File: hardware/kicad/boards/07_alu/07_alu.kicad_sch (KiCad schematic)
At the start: 0 parts

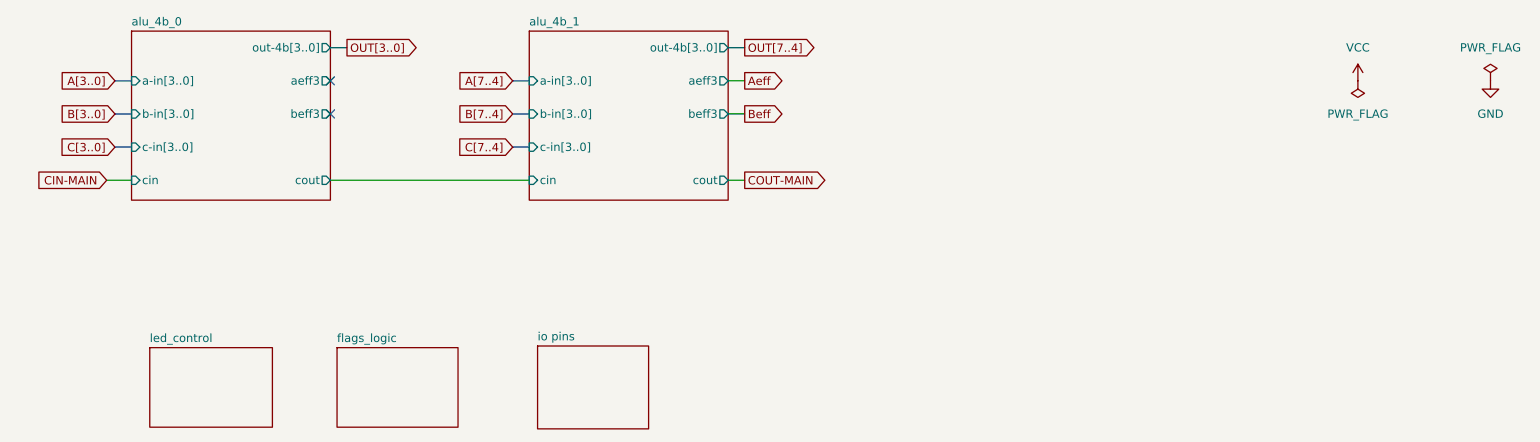
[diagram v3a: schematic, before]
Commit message: feat: route 8b ALU slice and annotate pending final signoff 🎉🎉
Highlights:
- 0 ERC/DRC errors
- 0 Unrouted nets
- 2345 track segments
- 388 vias after cleanup
- 760 pads
- 18 core 74xx chips
- 7 flag 74xx chips

Pending additional confirmation of hardware-simulation faithfulness and fidelity.
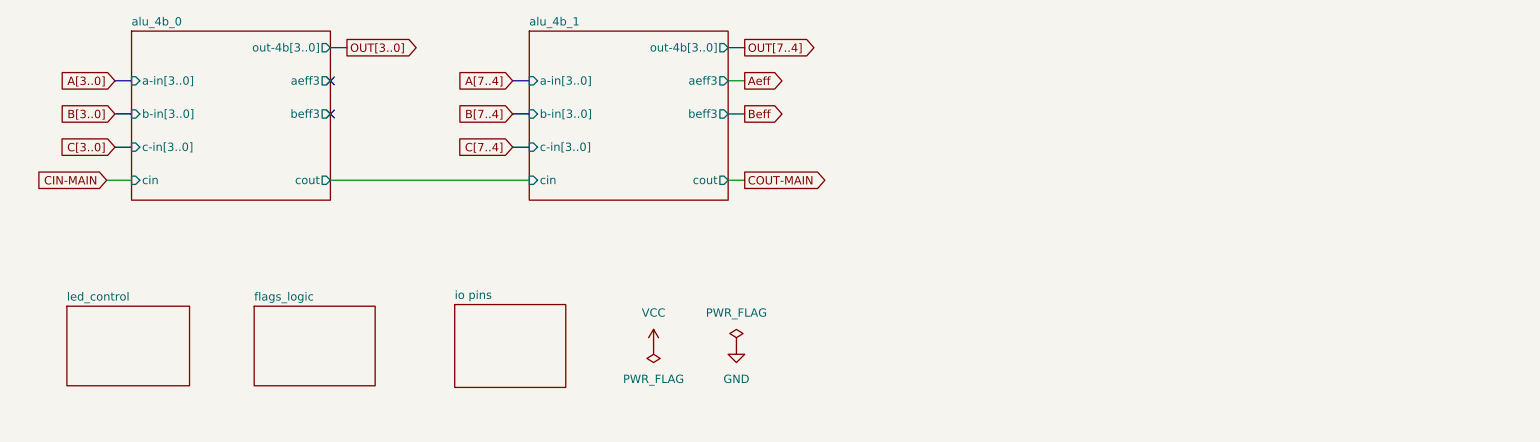
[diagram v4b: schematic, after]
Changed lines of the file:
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@@
 	(generator "eeschema")
 	(generator_version "10.0")
-	(paper "A4")
+	(paper "A5")
 	(no_connect
 		(at 63.5 40.64)
@@
 	(symbol
 		(lib_id "power:PWR_FLAG")
-		(at 220.98 35.56 180)
+		(at 125.73 76.2 0)
 		(unit 1)
 		(body_style 1)
@@
 		(dnp no)
 		(fields_autoplaced yes)
-		(property "Reference" "#FLG02"
-			(at 220.98 37.465 0)
+		(property "Reference" "#FLG01"
+			(at 125.73 74.295 0)
 			(hide yes)
 			(show_name no)
@@
 		)
 		(property "Value" "PWR_FLAG"
-			(at 220.98 40.64 0)
+			(at 125.73 71.12 0)
 			(show_name no)
 			(do_not_autoplace no)
@@
 		)
 		(property "Footprint" ""
-			(at 220.98 35.56 0)
+			(at 125.73 76.2 0)
 			(hide yes)
 			(show_name no)
@@
 		)
 		(property "Datasheet" ""
-			(at 220.98 35.56 0)
+			(at 125.73 76.2 0)
 			(hide yes)
 			(show_name no)
@@
 		)
 		(property "Description" "Special symbol for telling ERC where power comes from"
-			(at 220.98 35.56 0)
+			(at 125.73 76.2 0)
 			(hide yes)
 			(show_name no)
@@
 			(project "07_alu"
 				(path "/bf03590f-4078-420b-ac5f-55731d384371"
-					(reference "#FLG02")
+					(reference "#FLG01")
 					(unit 1)
 				)
@@
 	)
 	(symbol
-		(lib_id "power:VCC")
-		(at 220.98 35.56 0)
+		(lib_id "power:PWR_FLAG")
+		(at 113.03 76.2 180)
 		(unit 1)
 		(body_style 1)
@@
 		(dnp no)
 		(fields_autoplaced yes)
-		(property "Reference" "#PWR01"
-			(at 220.98 39.37 0)
-			(hide yes)
-			(show_name no)
-			(do_not_autoplace no)
-			(effects
-				(font
-					(size 1.27 1.27)
-				)
-			)
-		)
-		(property "Value" "VCC"
-			(at 220.98 30.48 0)
+		(property "Reference" "#FLG02"
+			(at 113.03 78.105 0)
+			(hide yes)
+			(show_name no)
+			(do_not_autoplace no)
+			(effects
+				(font
+					(size 1.27 1.27)
+				)
+			)
+		)
+		(property "Value" "PWR_FLAG"
+			(at 113.03 81.28 0)
 			(show_name no)
 			(do_not_autoplace no)
@@
 		)
 		(property "Footprint" ""
-			(at 220.98 35.56 0)
+			(at 113.03 76.2 0)
 			(hide yes)
 			(show_name no)
@@
 		)
 		(property "Datasheet" ""
-			(at 220.98 35.56 0)
-			(hide yes)
-			(show_name no)
-			(do_not_autoplace no)
-			(effects
-				(font
-					(size 1.27 1.27)
-				)
-			)
-		)
-		(property "Description" "Power symbol creates a global label with name \"VCC\""
-			(at 220.98 35.56 0)
+			(at 113.03 76.2 0)
+			(hide yes)
+			(show_name no)
+			(do_not_autoplace no)
+			(effects
+				(font
+					(size 1.27 1.27)
+				)
+			)
+		)
+		(property "Description" "Special symbol for telling ERC where power comes from"
+			(at 113.03 76.2 0)
 			(hide yes)
 			(show_name no)
@@
 			(project "07_alu"
 				(path "/bf03590f-4078-420b-ac5f-55731d384371"
-					(reference "#PWR01")
+					(reference "#FLG02")
 					(unit 1)
 				)
@@
 	)
 	(symbol
-		(lib_id "power:GND")
-		(at 241.3 35.56 0)
+		(lib_id "power:VCC")
+		(at 113.03 76.2 0)
 		(unit 1)
 		(body_style 1)
@@
 		(dnp no)
 		(fields_autoplaced yes)
-		(property "Reference" "#PWR02"
-			(at 241.3 41.91 0)
-			(hide yes)
-			(show_name no)
-			(do_not_autoplace no)
-			(effects
-				(font
-					(size 1.27 1.27)
-				)
-			)
-		)
-		(property "Value" "GND"
-			(at 241.3 40.64 0)
+		(property "Reference" "#PWR01"
+			(at 113.03 80.01 0)
+			(hide yes)
+			(show_name no)
+			(do_not_autoplace no)
+			(effects
+				(font
+					(size 1.27 1.27)
+				)
+			)
+		)
+		(property "Value" "VCC"
+			(at 113.03 71.12 0)
 			(show_name no)
 			(do_not_autoplace no)
@@
 		)
 		(property "Footprint" ""
-			(at 241.3 35.56 0)
+			(at 113.03 76.2 0)
 			(hide yes)
 			(show_name no)
@@
 		)
 		(property "Datasheet" ""
-			(at 241.3 35.56 0)
-			(hide yes)
-			(show_name no)
-			(do_not_autoplace no)
-			(effects
-				(font
-					(size 1.27 1.27)
-				)
-			)
-		)
-		(property "Description" "Power symbol creates a global label with name \"GND\" , ground"
-			(at 241.3 35.56 0)
+			(at 113.03 76.2 0)
+			(hide yes)
+			(show_name no)
+			(do_not_autoplace no)
+			(effects
+				(font
+					(size 1.27 1.27)
+				)
+			)
+		)
+		(property "Description" "Power symbol creates a global label with name \"VCC\""
+			(at 113.03 76.2 0)
 			(hide yes)
 			(show_name no)
@@
 			(project "07_alu"
 				(path "/bf03590f-4078-420b-ac5f-55731d384371"
-					(reference "#PWR02")
+					(reference "#PWR01")
 					(unit 1)
 				)
@@
 	)
 	(symbol
-		(lib_id "power:PWR_FLAG")
-		(at 241.3 35.56 0)
+		(lib_id "power:GND")
+		(at 125.73 76.2 0)
 		(unit 1)
 		(body_style 1)
@@
 		(dnp no)
 		(fields_autoplaced yes)
-		(property "Reference" "#FLG01"
-			(at 241.3 33.655 0)
-			(hide yes)
-			(show_name no)
-			(do_not_autoplace no)
-			(effects
-				(font
-					(size 1.27 1.27)
-				)
-			)
-		)
-		(property "Value" "PWR_FLAG"
-			(at 241.3 30.48 0)
+		(property "Reference" "#PWR02"
+			(at 125.73 82.55 0)
+			(hide yes)
+			(show_name no)
+			(do_not_autoplace no)
+			(effects
+				(font
+					(size 1.27 1.27)
+				)
+			)
+		)
+		(property "Value" "GND"
+			(at 125.73 81.28 0)
 			(show_name no)
 			(do_not_autoplace no)
@@
 		)
 		(property "Footprint" ""
-			(at 241.3 35.56 0)
+			(at 125.73 76.2 0)
 			(hide yes)
 			(show_name no)
@@
 		)
 		(property "Datasheet" ""
-			(at 241.3 35.56 0)
-			(hide yes)
-			(show_name no)
-			(do_not_autoplace no)
-			(effects
-				(font
-					(size 1.27 1.27)
-				)
-			)
-		)
-		(property "Description" "Special symbol for telling ERC where power comes from"
-			(at 241.3 35.56 0)
+			(at 125.73 76.2 0)
+			(hide yes)
+			(show_name no)
+			(do_not_autoplace no)
+			(effects
+				(font
+					(size 1.27 1.27)
+				)
+			)
+		)
+		(property "Description" "Power symbol creates a global label with name \"GND\" , ground"
+			(at 125.73 76.2 0)
 			(hide yes)
 			(show_name no)
@@
 			(project "07_alu"
 				(path "/bf03590f-4078-420b-ac5f-55731d384371"
-					(reference "#FLG01")
+					(reference "#PWR02")
 					(unit 1)
 				)
@@
 	)
 	(sheet
-		(at 35.814 76.454)
+		(at 23.114 70.104)
 		(size 18.796 12.192)
 		(exclude_from_sim no)
@@
 		)
 		(property "Sheetname" "led_control"
-			(at 35.814 75.7424 0)
+			(at 23.114 69.3924 0)
 			(show_name no)
 			(do_not_autoplace no)
@@
 		)
 		(property "Sheetfile" "led_unit.kicad_sch"
-			(at 35.814 89.2306 0)
+			(at 23.114 82.8806 0)
 			(hide yes)
 			(show_name no)
@@
 	)
 	(sheet
-		(at 64.516 76.454)
+		(at 51.816 70.104)
 		(size 18.542 12.192)
 		(exclude_from_sim no)
@@
 		)
 		(property "Sheetname" "flags_logic"
-			(at 64.516 75.7424 0)
+			(at 51.816 69.3924 0)
 			(show_name no)
 			(do_not_autoplace no)
@@
 		)
 		(property "Sheetfile" "flags_logic.kicad_sch"
-			(at 64.516 89.2306 0)
+			(at 51.816 82.8806 0)
 			(hide yes)
 			(show_name no)
@@
 	)
 	(sheet
-		(at 95.25 76.2)
+		(at 82.55 69.85)
 		(size 17.018 12.7)
 		(exclude_from_sim no)
@@
 		)
 		(property "Sheetname" "io pins"
-			(at 95.25 75.4884 0)
+			(at 82.55 69.1384 0)
 			(show_name no)
 			(do_not_autoplace no)
@@
 		)
 		(property "Sheetfile" "iopins.kicad_sch"
-			(at 95.25 89.4846 0)
-			(hide yes)
-			(show_name no)
+			(at 82.55 83.1346 0)
+			(hide yes)
+			(show_name no)

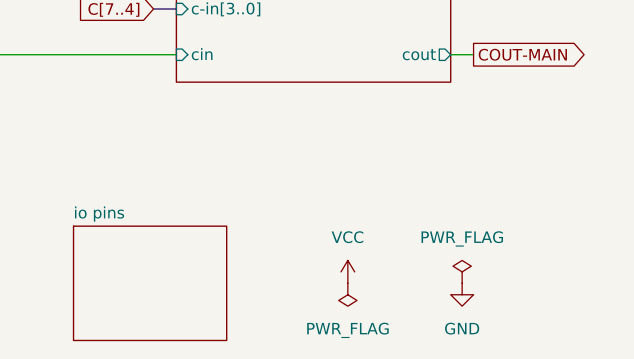
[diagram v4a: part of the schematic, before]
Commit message: fix: placed power flags to resolve flag error in kicad
DRC/ERC are both 0 :)
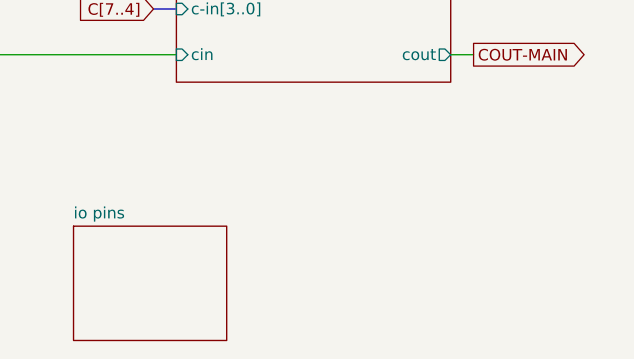
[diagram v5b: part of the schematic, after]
